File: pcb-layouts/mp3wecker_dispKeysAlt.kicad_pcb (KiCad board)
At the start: 2 copper layers, 93 x 48 mm, 46 parts, among them J2 Arduino, Q1 BC337, Q2 BC337, Q3 BC337, Q4 BC337, Q5 BC337, Q6 BC337, SW1 SW_Push_SPDT, U1 4511, U3 MCP23008-xP, U9 4017

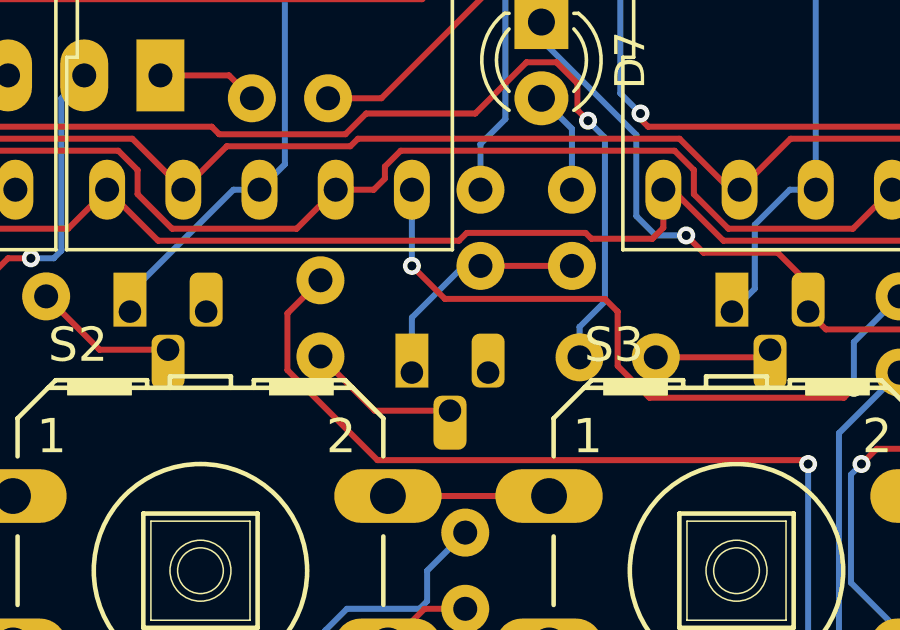
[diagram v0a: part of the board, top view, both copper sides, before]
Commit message: Erste Version mit alternativem Display
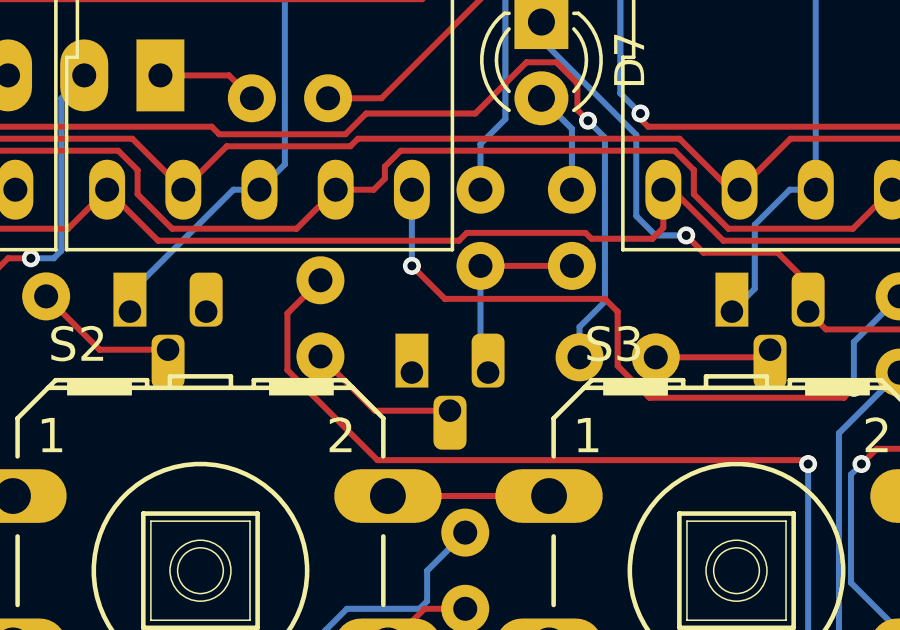
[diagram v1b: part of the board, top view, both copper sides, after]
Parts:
- Q1: value BC337 -> BC327
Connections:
- Q1 pad 1: Net-(Q1-C) -> +5V
- Q1 pad 3: GND -> Net-(Q1-E)
- R13 pad 1: Net-(Q1-C) -> Net-(Q1-E)
- R14 pad 1: Net-(Q1-C) -> Net-(Q1-E)
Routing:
- net Net-(Q1-C): track 7.72 -> 0.00 mm
- net Net-(Q1-E): track 0.00 -> 6.71 mm
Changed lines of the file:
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@@
   (net 33 "Net-(D8-A)")
   (net 34 "Net-(D9-A)")
-  (net 35 "Net-(Q1-C)")
+  (net 35 "Net-(Q1-E)")
   (net 36 "Net-(D2-DP)")
   (net 37 "Net-(U9-Q0)")
@@
       (stroke (width 0.1) (type solid)) (fill none) (layer "B.Fab"))
     (pad "1" thru_hole circle (at 0 0 90) (size 1.6 1.6) (drill 0.8) (layers "*.Cu" "*.Mask")
-      (net 35 "Net-(Q1-C)") (pintype "passive"))
+      (net 35 "Net-(Q1-E)") (pintype "passive"))
     (pad "2" thru_hole oval (at 2.54 0 90) (size 1.6 1.6) (drill 0.8) (layers "*.Cu" "*.Mask")
       (net 52 "Net-(D6-A)") (pintype "passive"))
@@
       (stroke (width 0.1) (type solid)) (fill none) (layer "B.Fab"))
     (pad "1" thru_hole circle (at 0 0 90) (size 1.6 1.6) (drill 0.8) (layers "*.Cu" "*.Mask")
-      (net 35 "Net-(Q1-C)") (pintype "passive"))
+      (net 35 "Net-(Q1-E)") (pintype "passive"))
     (pad "2" thru_hole oval (at 2.54 0 90) (size 1.6 1.6) (drill 0.8) (layers "*.Cu" "*.Mask")
       (net 53 "Net-(D7-A)") (pintype "passive"))
@@
     (property "Sheetfile" "mp3wecker_dispKeysAlt.kicad_sch")
     (property "Sheetname" "")
-    (property "ki_description" "NPN TO-92 transistor, 45V, 800mA, 625mW, Complementary to BC327, Alternate KiCAD Library")
-    (property "ki_keywords" "transistor NPN BC337")
+    (property "ki_description" "PNP TO-92 transistor, 45V, 0.8A, 625mW, Complementary to BC337, Alternate KiCAD Library")
+    (property "ki_keywords" "transistor PNP BC327")
     (attr through_hole)
     (fp_text reference "Q1" (at 1.27 3.8) (layer "B.SilkS")
         (effects (font (size 1 1) (thickness 0.15)) (justify mirror))
     )
-    (fp_text value "BC337" (at 1.27 -2.79) (layer "B.Fab")
+    (fp_text value "BC327" (at 1.27 -2.79) (layer "B.Fab")
         (effects (font (size 1 1) (thickness 0.15)) (justify mirror))
     )
@@
       (stroke (width 0.1) (type solid)) (layer "B.Fab"))
     (pad "1" thru_hole rect (at 0 0) (size 1.1 1.8) (drill 0.75 (offset 0 -0.4)) (layers "*.Cu" "*.Mask")
-      (net 35 "Net-(Q1-C)") (pinfunction "C") (pintype "passive"))
+      (net 16 "+5V") (pinfunction "C") (pintype "passive"))
     (pad "2" thru_hole roundrect (at 1.27 1.27) (size 1.1 1.8) (drill 0.75 (offset 0 0.4)) (layers "*.Cu" "*.Mask") (roundrect_rratio 0.25)
       (net 17 "Net-(Q1-B)") (pinfunction "B") (pintype "input"))
     (pad "3" thru_hole roundrect (at 2.54 0) (size 1.1 1.8) (drill 0.75 (offset 0 -0.4)) (layers "*.Cu" "*.Mask") (roundrect_rratio 0.25)
-      (net 23 "GND") (pinfunction "E") (pintype "passive"))
+      (net 35 "Net-(Q1-E)") (pinfunction "E") (pintype "passive"))
     (model "${KICAD6_3DMODEL_DIR}/Package_TO_SOT_THT.3dshapes/TO-92L.wrl"
       (offset (xyz 0 0 0))
@@
     )
     (stroke (width 0.05) (type solid)) (fill none) (layer "Edge.Cuts"))
-  (gr_text_box "mp3Wecker\nSmallhill 26.3"
+  (gr_text_box "mp3Wecker\nSmallhill 26.4"
     (start 111.125 112.268) (end 130.175 117.856) (layer "F.Cu")
       (effects (font (size 1.5 1.5) (thickness 0.3) bold) (justify left top))
@@
   (segment (start 151.214 104.818) (end 150.114 105.918) (width 0.2) (layer "B.Cu") (net 34))
   (segment (start 133.096 94.488) (end 136.144 94.488) (width 0.2) (layer "F.Cu") (net 35))
-  (segment (start 130.81 96.208315) (end 132.813158 94.205157) (width 0.2) (layer "B.Cu") (net 35))
-  (segment (start 130.81 98.044) (end 130.81 96.208315) (width 0.2) (layer "B.Cu") (net 35))
+  (segment (start 133.35 98.044) (end 133.096 97.79) (width 0.2) (layer "B.Cu") (net 35))
+  (segment (start 133.096 97.79) (end 133.096 94.488) (width 0.2) (layer "B.Cu") (net 35))
   (segment (start 131.91 95.588) (end 137.244 95.588) (width 0.2) (layer "F.Cu") (net 36))
   (segment (start 145.212 98.882) (end 145.542 98.552) (width 0.2) (layer "F.Cu") (net 36))
